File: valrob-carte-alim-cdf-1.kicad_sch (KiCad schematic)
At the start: 21 parts, among them J1 USB_C_Receptacle_USB2.0_14P, J4 Conn_01x04_Pin, J6 Conn_01x04_Pin, SW1 SW_Push, SW2 SW_Push, U4 ESP32-S3-WROOM-1

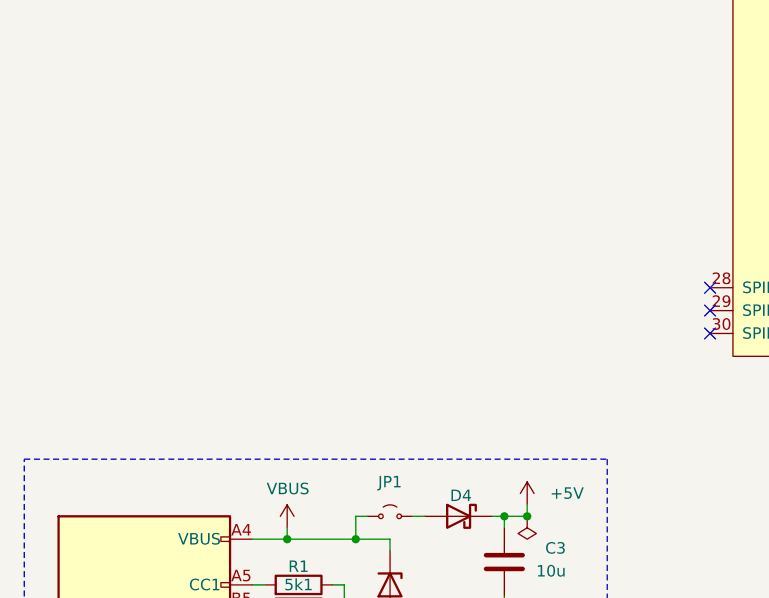
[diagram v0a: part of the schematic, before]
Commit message: schem: add TLV757P 3.3v LDO
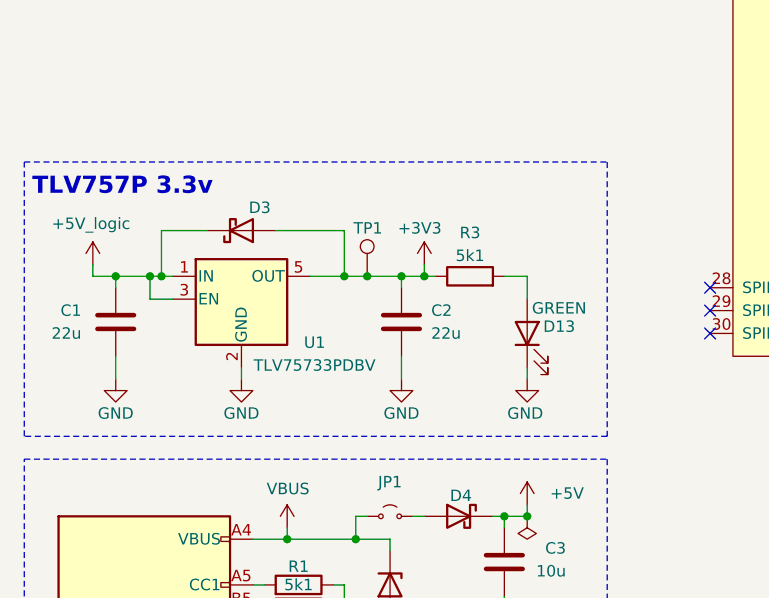
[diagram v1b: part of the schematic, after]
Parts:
- added C1, C2: 22u, Capacitor_SMD:C_0603_1608Metric, symbol Device:C
- added D13: GREEN, LED_SMD:LED_0805_2012Metric, symbol Device:LED
- added D3: D_Schottky, Diode_SMD:D_SMA, symbol Device:D_Schottky
- added R3: 5k1, Resistor_SMD:R_0402_1005Metric, symbol Device:R
- added TP1: TestPoint, TestPoint:TestPoint_Pad_D2.0mm, symbol Connector:TestPoint
- added U1: TLV75733PDBV, Package_TO_SOT_SMD:SOT-23-5, symbol Regulator_Linear:TLV75733PDBV
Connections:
- net +3V3: now also C2.2, D3.2 (A), R3.1, TP1.1, U1.5 (OUT)
- net GND: now also C1.1, C2.1, D13.1 (K), U1.2 (GND)
- new net: D13.2 (A), R3.2
- new net +5V_logic: C1.2, D3.1 (K), U1.1 (IN), U1.3 (EN)
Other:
- note added: "TLV757P 3.3v"

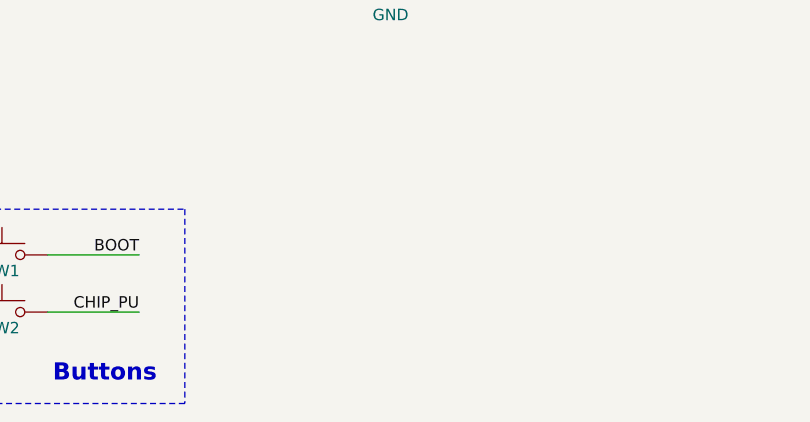
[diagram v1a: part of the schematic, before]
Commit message: schem: add +BATT voltage sense
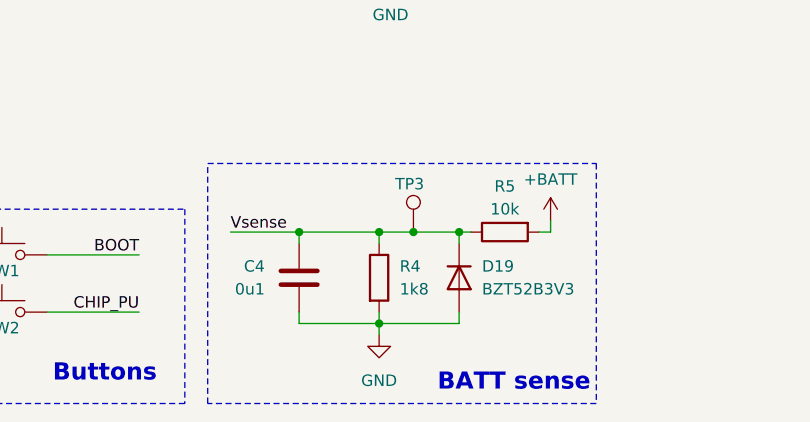
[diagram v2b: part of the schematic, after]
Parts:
- added C4: 0u1, Capacitor_SMD:C_0402_1005Metric, symbol Device:C
- added D19: BZT52B3V3, Diode_SMD:D_SOD-123, symbol Device:D
- added R4: 1k8, Resistor_SMD:R_0603_1608Metric, symbol Device:R
- added R5: 10k, Resistor_SMD:R_0402_1005Metric, symbol Device:R
- added TP3: TestPoint, TestPoint:TestPoint_Pad_D2.0mm, symbol Connector:TestPoint
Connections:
- net GND: now also C4.2, D19.2 (A), R4.2
- new net +BATT: R5.2
- new net Vsense: C4.1, D19.1 (K), R4.1, R5.1, TP3.1
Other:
- note added: "BATT sense"

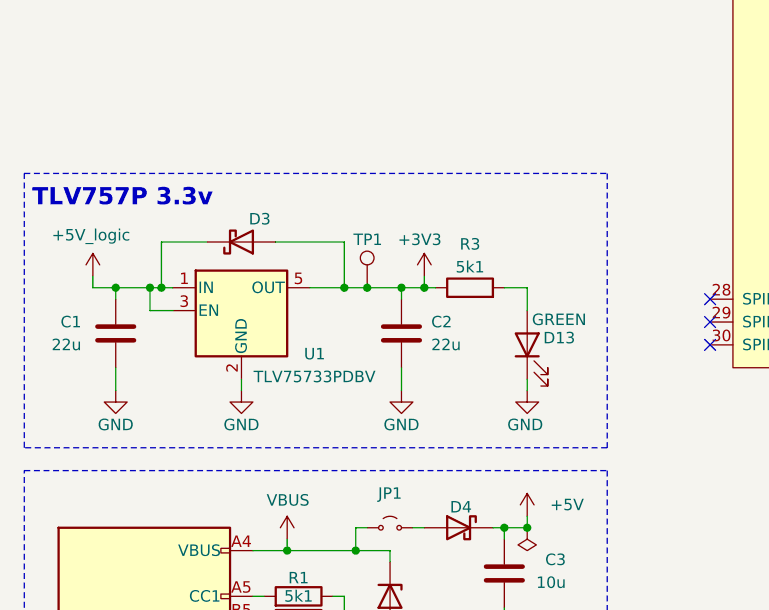
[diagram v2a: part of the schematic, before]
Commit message: schem: add CAN transceiver
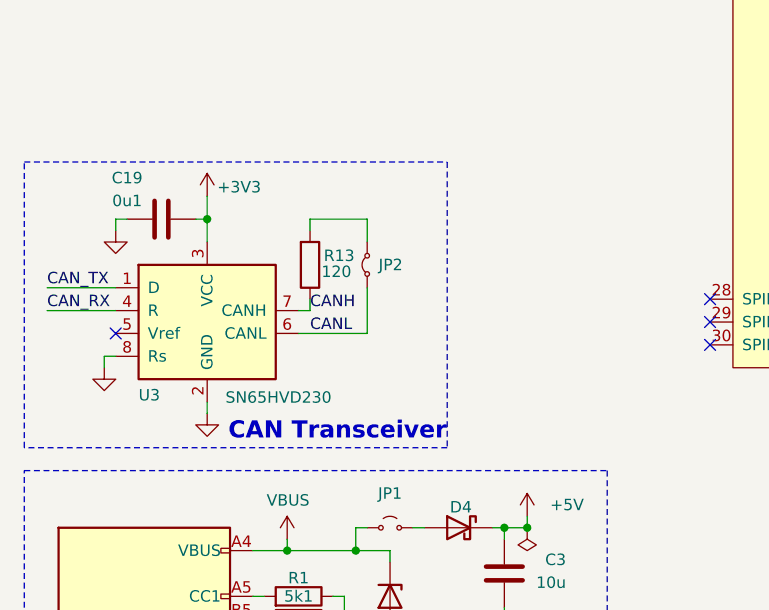
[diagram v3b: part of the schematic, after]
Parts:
- removed C1, C2: 22u, Capacitor_SMD:C_0603_1608Metric, symbol Device:C
- removed D13: GREEN, LED_SMD:LED_0805_2012Metric, symbol Device:LED
- removed D3: D_Schottky, Diode_SMD:D_SMA, symbol Device:D_Schottky
- removed R3: 5k1, Resistor_SMD:R_0402_1005Metric, symbol Device:R
- removed TP1: TestPoint, TestPoint:TestPoint_Pad_D2.0mm, symbol Connector:TestPoint
- removed U1: TLV75733PDBV, Package_TO_SOT_SMD:SOT-23-5, symbol Regulator_Linear:TLV75733PDBV
- added C19: 0u1, Capacitor_SMD:C_0402_1005Metric, symbol Device:C
- added JP2: Jumper_2_Small_Bridged, Jumper:SolderJumper-2_P1.3mm_Open_RoundedPad1.0x1.5mm, symbol Jumper:Jumper_2_Small_Bridged
- added R13: 120, Resistor_SMD:R_1206_3216Metric, symbol Device:R
- added U3: SN65HVD230, Package_SO:SOIC-8_3.9x4.9mm_P1.27mm, symbol Interface_CAN_LIN:SN65HVD230
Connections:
- net +3V3: now also C19.1, U3.3 (VCC)
- net GND: now also C19.2, U3.2 (GND), U3.8 (Rs)
- new net: JP2.2 (B), R13.2
- new net CANH: R13.1, U3.7 (CANH)
- new net CANL: JP2.1 (A), U3.6 (CANL)
- new net CAN_RX: U3.4 (R)
- new net CAN_TX: U3.1 (D)
- no-connect marks 9 -> 10
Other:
- note added: "CAN Transceiver"
- note removed: "TLV757P 3.3v"

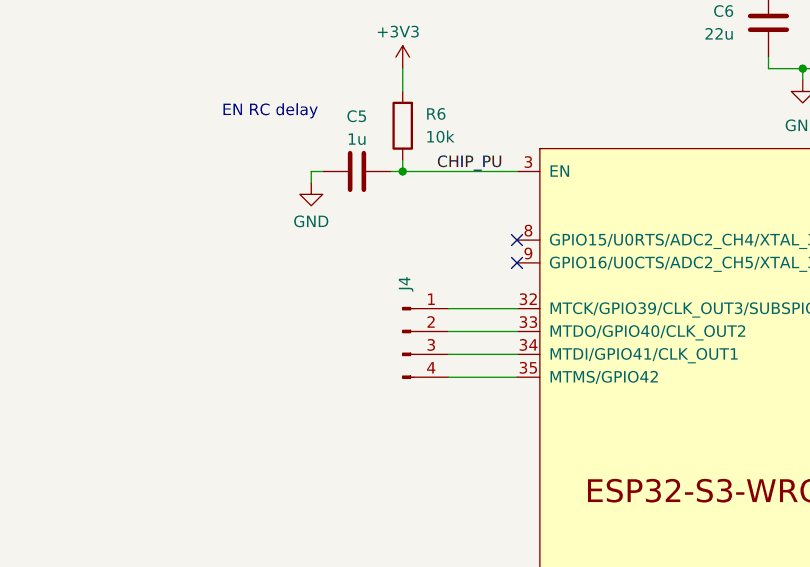
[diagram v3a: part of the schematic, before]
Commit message: schem: add additional connector for batt vin
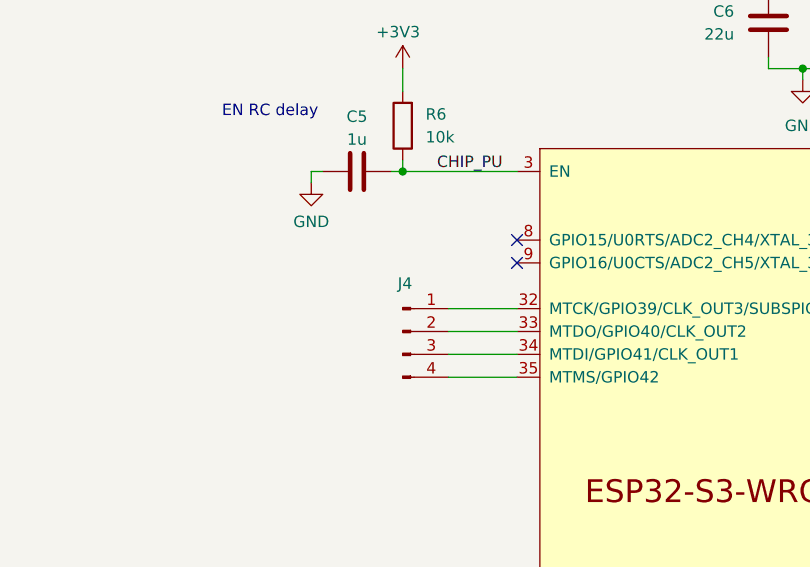
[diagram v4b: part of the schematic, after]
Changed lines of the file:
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@@
 		(dnp no)
 		(property "Reference" "J4"
-			(at 78.994 81.026 90)
+			(at 78.994 81.026 0)
 			(effects
 				(font

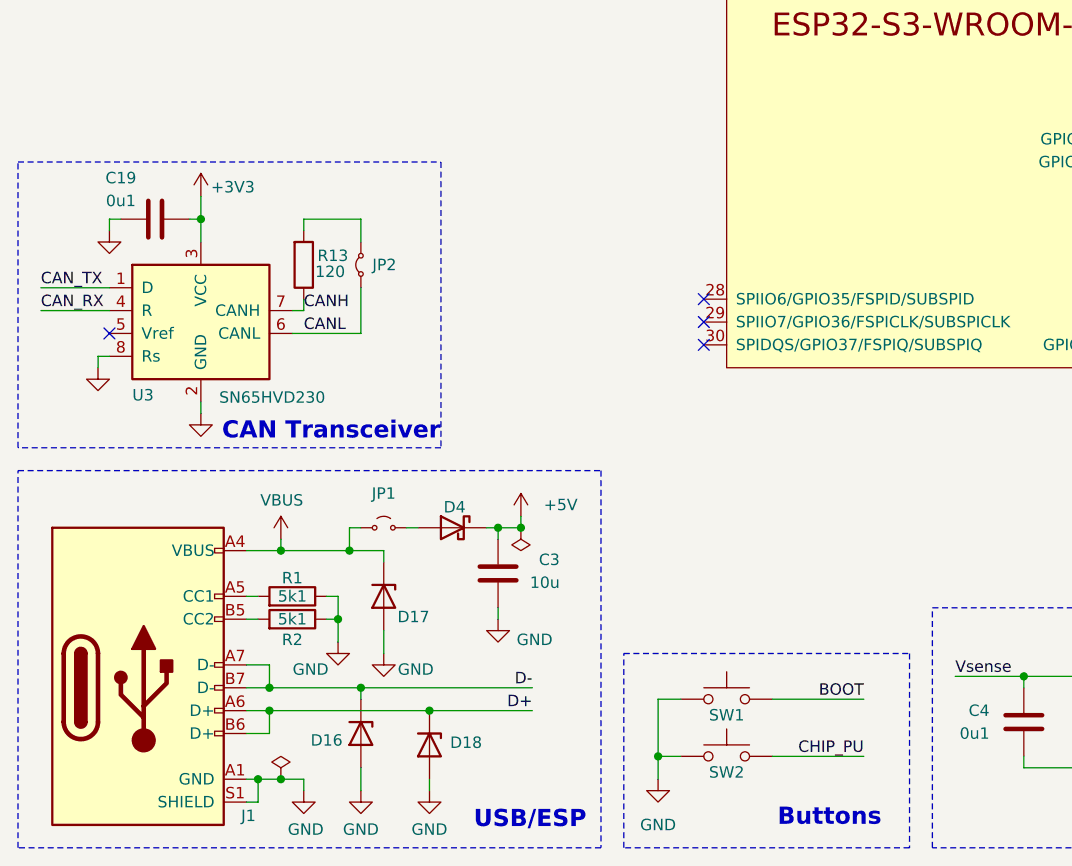
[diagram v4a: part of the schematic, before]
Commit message: schem: add BAU
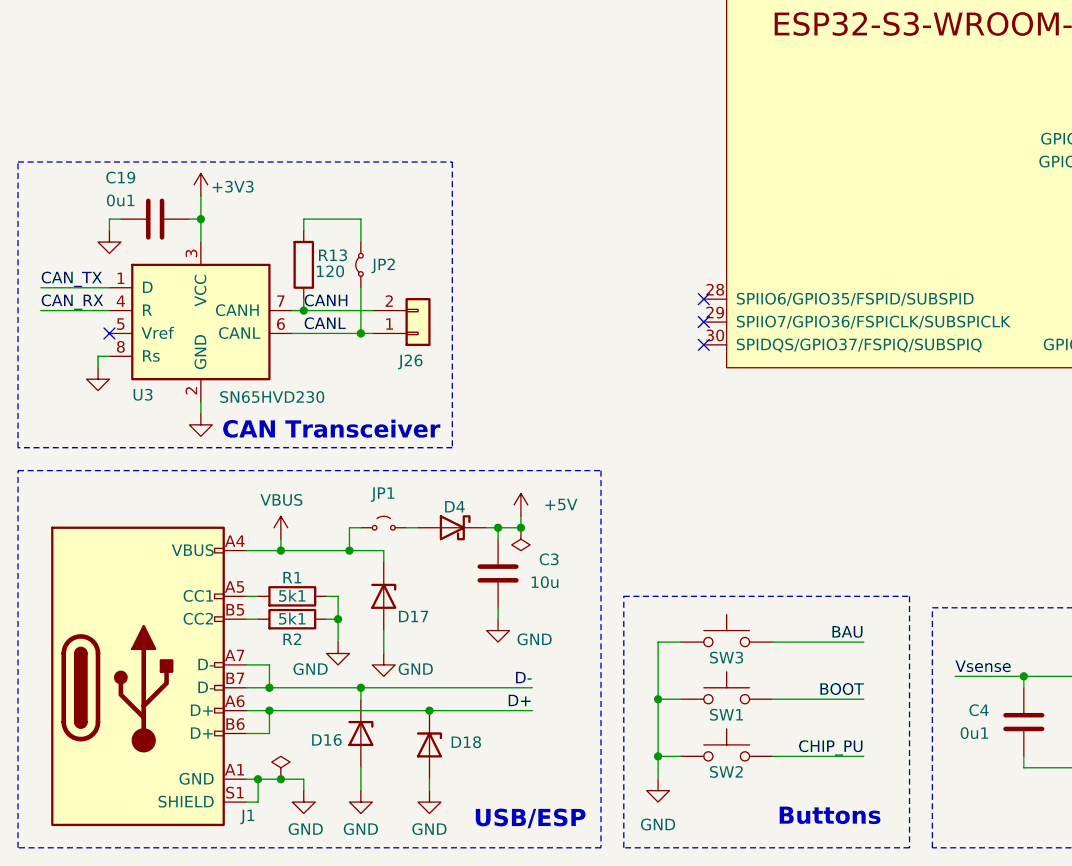
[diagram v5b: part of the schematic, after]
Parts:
- added J26: Conn_01x02, Connector_JST:JST_XH_B2B-XH-A_1x02_P2.50mm_Vertical, symbol Connector_Generic:Conn_01x02
- added SW3: SW_Push, Connector_JST:JST_XH_B2B-XH-A_1x02_P2.50mm_Vertical, symbol Switch:SW_Push
- SW1, SW2: footprint Button_Switch_SMD:SW_SPST_TS-1088-xR020 -> Connector_JST:JST_XH_B2B-XH-A_1x02_P2.50mm_Vertical; Basic Y -> Z; JLCPCB Part # C720477 -> C158012; Manufacturer XUNPU -> JST; Manufacturer Part Number TS-1088-AR02016 -> B2B-XH-A(LF)(SN)
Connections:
- net CANH: now also J26.2 (Pin_2)
- net CANL: now also J26.1 (Pin_1)
- net GND: now also SW3.1
- new net BAU: SW3.2

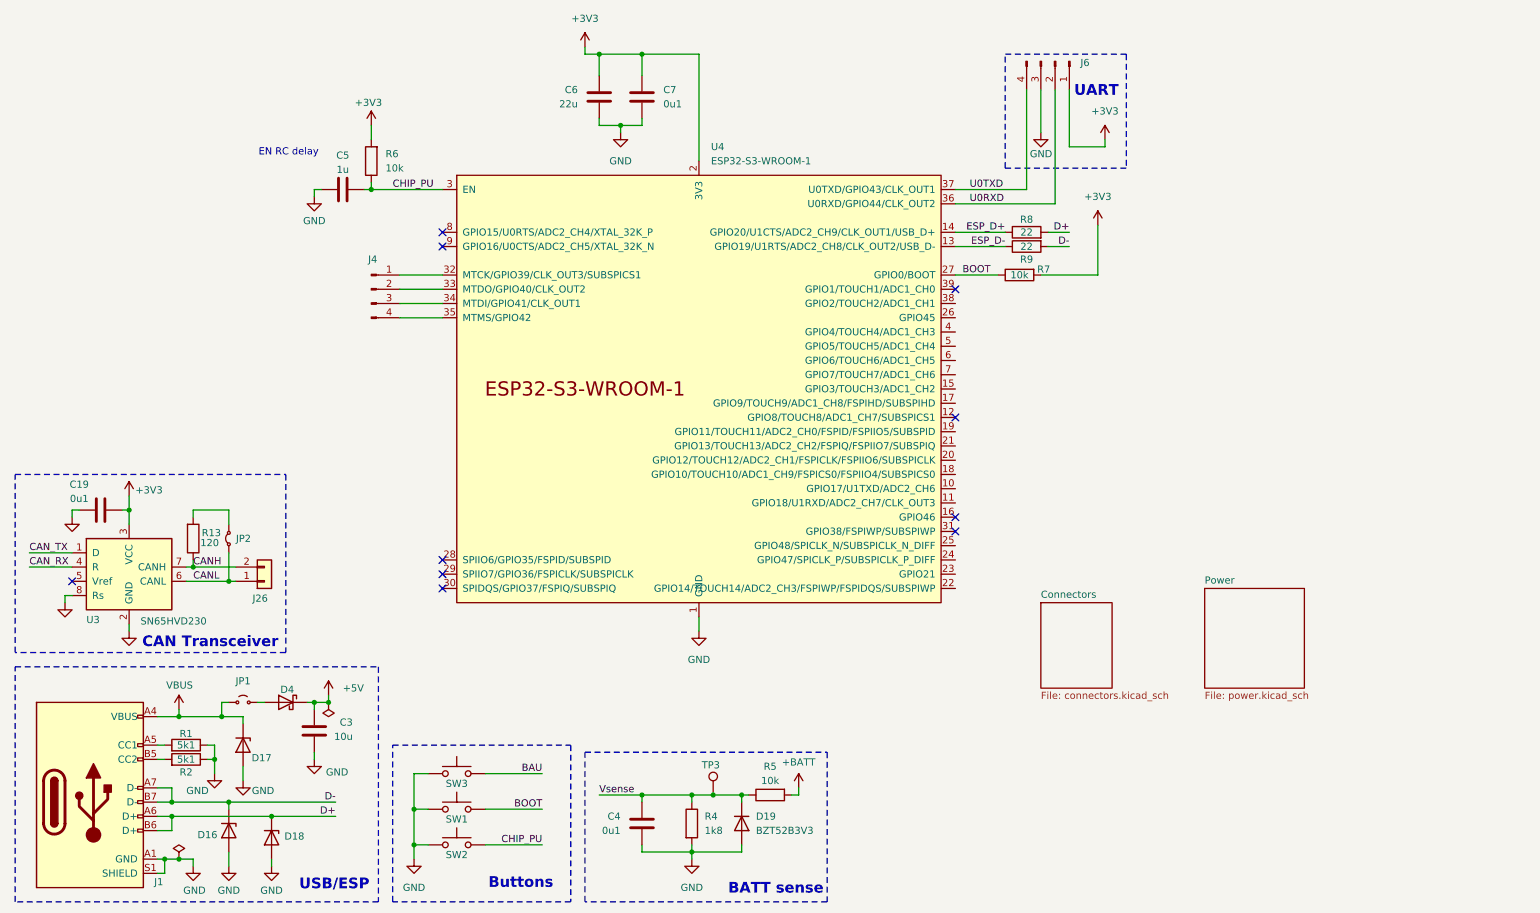
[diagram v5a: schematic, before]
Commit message: schem: add esp32 gpio connections
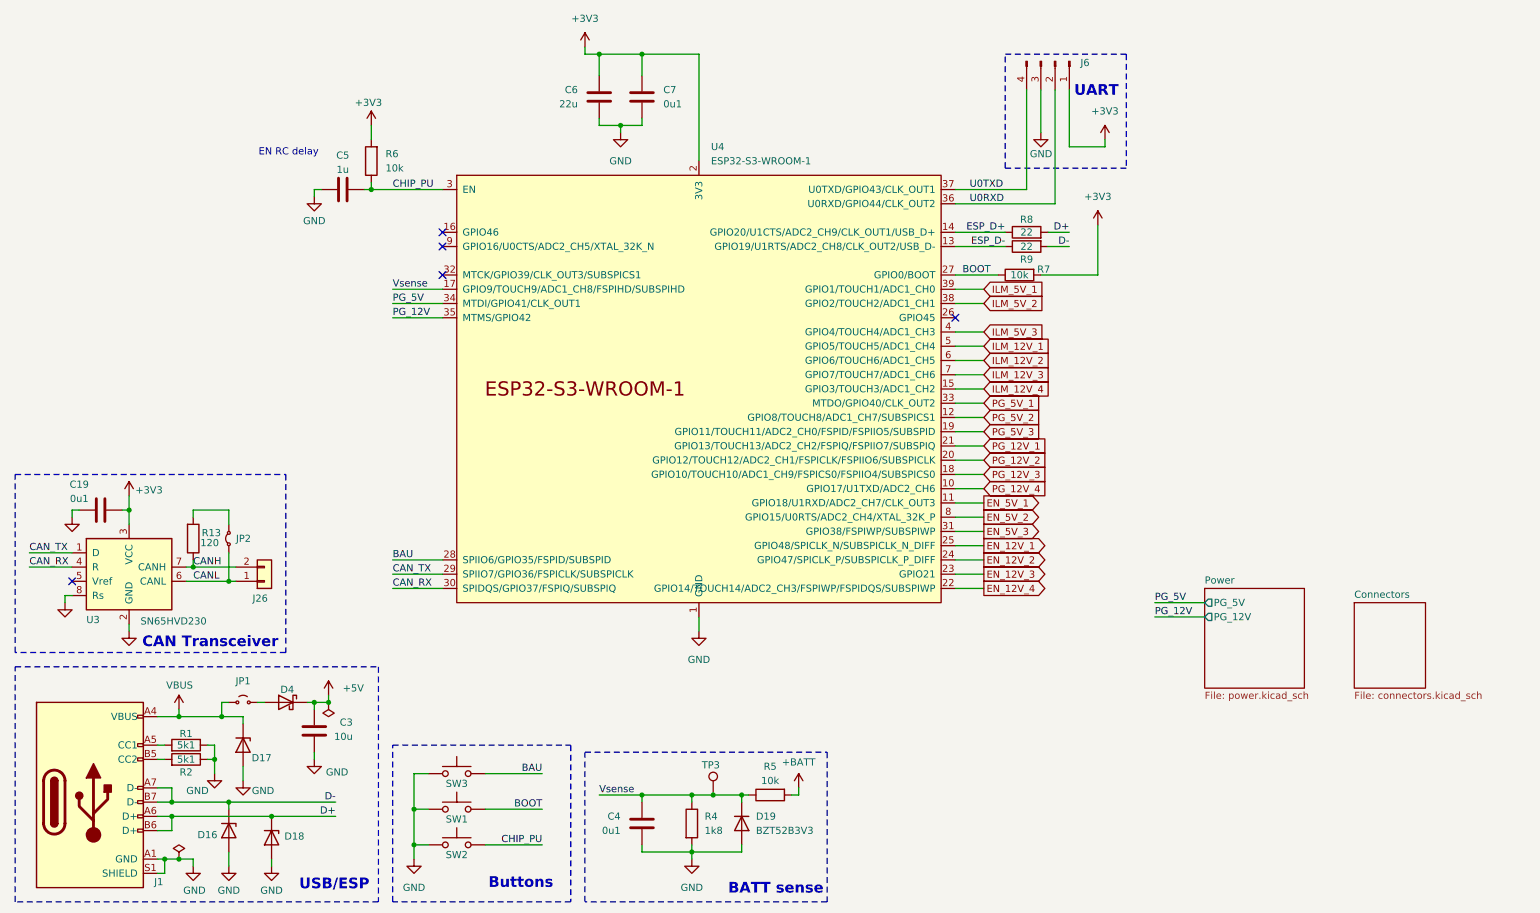
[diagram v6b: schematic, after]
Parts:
- removed J4: Conn_01x04_Pin, Connector_PinHeader_2.54mm:PinHeader_1x04_P2.54mm_Vertical, symbol Connector:Conn_01x04_Pin
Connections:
- net BAU: now also U4.28 (SPIIO6/GPIO35/FSPID/SUBSPID)
- net CAN_RX: now also U4.30 (SPIDQS/GPIO37/FSPIQ/SUBSPIQ)
- net CAN_TX: now also U4.29 (SPIIO7/GPIO36/FSPICLK/SUBSPICLK)
- net Vsense: now also U4.17 (GPIO9/TOUCH9/ADC1_CH8/FSPIHD/SUBSPIHD)
- net PG_12V_4: now reaches U4.10 (GPIO17/U1TXD/ADC2_CH6)
- net EN_5V_1: now reaches U4.11 (GPIO18/U1RXD/ADC2_CH7/CLK_OUT3)
- net PG_5V_2: now reaches U4.12 (GPIO8/TOUCH8/ADC1_CH7/SUBSPICS1)
- net ILM_12V_4: now reaches U4.15 (GPIO3/TOUCH3/ADC1_CH2)
- net PG_12V_3: now reaches U4.18 (GPIO10/TOUCH10/ADC1_CH9/FSPICS0/FSPIIO4/SUBSPICS0)
- net PG_5V_3: now reaches U4.19 (GPIO11/TOUCH11/ADC2_CH0/FSPID/FSPIIO5/SUBSPID)
- net PG_12V_2: now reaches U4.20 (GPIO12/TOUCH12/ADC2_CH1/FSPICLK/FSPIIO6/SUBSPICLK)
- net PG_12V_1: now reaches U4.21 (GPIO13/TOUCH13/ADC2_CH2/FSPIQ/FSPIIO7/SUBSPIQ)
- net EN_12V_4: now reaches U4.22 (GPIO14/TOUCH14/ADC2_CH3/FSPIWP/FSPIDQS/SUBSPIWP)
- net EN_12V_3: now reaches U4.23 (GPIO21)
- net EN_12V_2: now reaches U4.24 (GPIO47/SPICLK_P/SUBSPICLK_P_DIFF)
- net EN_12V_1: now reaches U4.25 (GPIO48/SPICLK_N/SUBSPICLK_N_DIFF)
- net EN_5V_3: now reaches U4.31 (GPIO38/FSPIWP/SUBSPIWP)
- net PG_5V_1: now reaches U4.33 (MTDO/GPIO40/CLK_OUT2)
- net PG_5V: now reaches U4.34 (MTDI/GPIO41/CLK_OUT1)
- net PG_12V: now reaches U4.35 (MTMS/GPIO42)
- net ILM_5V_2: now reaches U4.38 (GPIO2/TOUCH2/ADC1_CH1)
- net ILM_5V_1: now reaches U4.39 (GPIO1/TOUCH1/ADC1_CH0)
- net ILM_5V_3: now reaches U4.4 (GPIO4/TOUCH4/ADC1_CH3)
- net ILM_12V_1: now reaches U4.5 (GPIO5/TOUCH5/ADC1_CH4)
- net ILM_12V_2: now reaches U4.6 (GPIO6/TOUCH6/ADC1_CH5)
- net ILM_12V_3: now reaches U4.7 (GPIO7/TOUCH7/ADC1_CH6)
- net EN_5V_2: now reaches U4.8 (GPIO15/U0RTS/ADC2_CH4/XTAL_32K_P)
- no-connect marks 10 -> 5
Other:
- sheet Power ports: added PG_12V, PG_5V; removed none
